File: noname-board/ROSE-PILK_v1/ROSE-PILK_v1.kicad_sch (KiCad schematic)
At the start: 2 parts, among them J2 Conn_01x03, SW1 SW_Push

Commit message: dual rp2040z
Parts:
- added J2: Conn_01x03, Connector_PinHeader_2.00mm:PinHeader_1x03_P2.00mm_Horizontal, symbol Connector_Generic:Conn_01x03
- added SW2: SW_Push, PS1024ALRED:SW_PS1024ALRED, symbol Switch:SW_Push
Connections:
- net GND: now also J2.2 (Pin_2), SW2.2
- net RP2040/SWCLK renamed SWDIO-A
- net RP2040/SWDIO renamed SWCLK-A
- new net RP2041/~{RST}: SW2.1
- new net SWCLK-B: J2.1 (Pin_1)
- new net SWDIO-B: J2.3 (Pin_3)
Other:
- added sheet BOOTSEL1 (BOOTSEL.kicad_sch)
- added sheet Flash Memory1 (flash.kicad_sch)
- added sheet RP2040-Connect (RP2040-Connect.kicad_sch)
- added sheet RP2041 (RP2040.kicad_sch)
- sheet USBC ports: added A-USB_D+, A-USB_D-, B-USB_D+, B-USB_D-; removed USB_D+, USB_D-
- note added: "RP2040-A"
- note added: "RP2040-A Comm Pins"
- note added: "RP2040-B"
- note added: "RP2040-B Comm Pins"
- note added: "SD Card Reader"
- moved on the sheet: J2

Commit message: Schematics
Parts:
- J2: footprint Connector_PinHeader_2.00mm:PinHeader_1x03_P2.00mm_Horizontal -> Connector_PinHeader_2.00mm:PinHeader_1x03_P2.00mm_Vertical
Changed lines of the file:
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@@
       (effects (font (size 1.27 1.27)))
     )
-    (property "Footprint" "Connector_PinHeader_2.00mm:PinHeader_1x03_P2.00mm_Horizontal" (at 270.51 73.66 0)
+    (property "Footprint" "Connector_PinHeader_2.00mm:PinHeader_1x03_P2.00mm_Vertical" (at 270.51 73.66 0)
       (effects (font (size 1.27 1.27)) hide)
     )
@@
       (effects (font (size 1.27 1.27)))
     )
-    (property "Footprint" "Connector_PinHeader_2.00mm:PinHeader_1x03_P2.00mm_Horizontal" (at 60.96 74.93 0)
+    (property "Footprint" "Connector_PinHeader_2.00mm:PinHeader_1x03_P2.00mm_Vertical" (at 60.96 74.93 0)
       (effects (font (size 1.27 1.27)) hide)
     )

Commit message: v1 functionality finished
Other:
- sheet USBC ports: added USB_5V; removed none
- sheet power ports: added USB_IN; removed none
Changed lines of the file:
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@@
+    (stroke (width 0) (type default))
+  )
+  (wire (pts (xy 36.83 72.39) (xy 41.91 72.39))
     (stroke (width 0) (type default))
   )
@@
   )
   (wire (pts (xy 68.58 111.76) (xy 81.28 111.76))
+    (stroke (width 0) (type default))
+  )
+  (wire (pts (xy 17.78 147.32) (xy 25.4 147.32))
     (stroke (width 0) (type default))
   )
@@
     (effects (font (size 1.27 1.27)) (justify right bottom))
   )
+  (label "USB_5V" (at 17.78 147.32 0) (fields_autoplaced)
+    (effects (font (size 1.27 1.27)) (justify left bottom))
+  )
   (label "3V3" (at 134.62 24.13 0) (fields_autoplaced)
     (effects (font (size 1.27 1.27)) (justify left bottom))
@@
   )
   (label "GPIO1-A" (at 175.26 27.94 0) (fields_autoplaced)
+    (effects (font (size 1.27 1.27)) (justify left bottom))
+  )
+  (label "USB_5V" (at 41.91 72.39 0) (fields_autoplaced)
     (effects (font (size 1.27 1.27)) (justify left bottom))
   )
@@
       (effects (font (size 1.27 1.27)) (justify right))
     )
+    (pin "USB_5V" input (at 36.83 72.39 0)
+      (effects (font (size 1.27 1.27)) (justify right))
+    )
     (instances
       (project "ROSE-PILK_v1"
@@
       (effects (font (size 1.27 1.27)) (justify left top))
     )
+    (pin "USB_IN" input (at 25.4 147.32 180)
+      (effects (font (size 1.27 1.27)) (justify left))
+    )
     (pin "5V" input (at 39.37 144.78 0)

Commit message: v1 functionality finished
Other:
- added sheet GPIO_Connect (GPIO_Connect.kicad_sch)

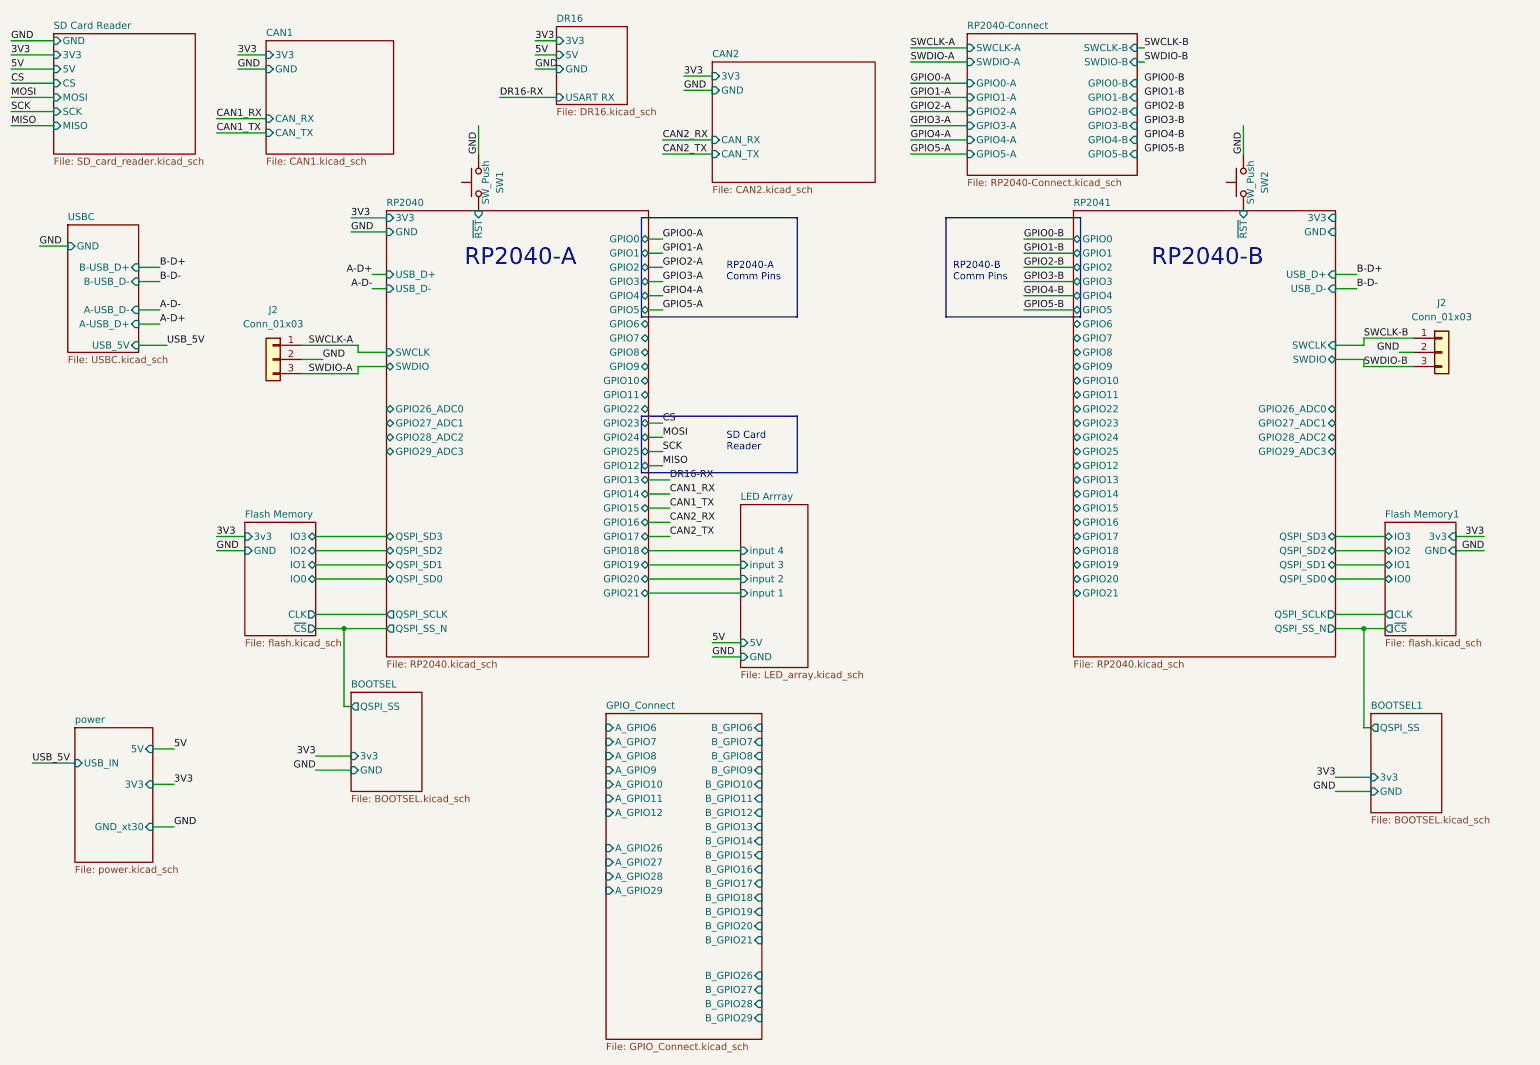
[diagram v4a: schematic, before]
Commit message: schematic finished, placement progress
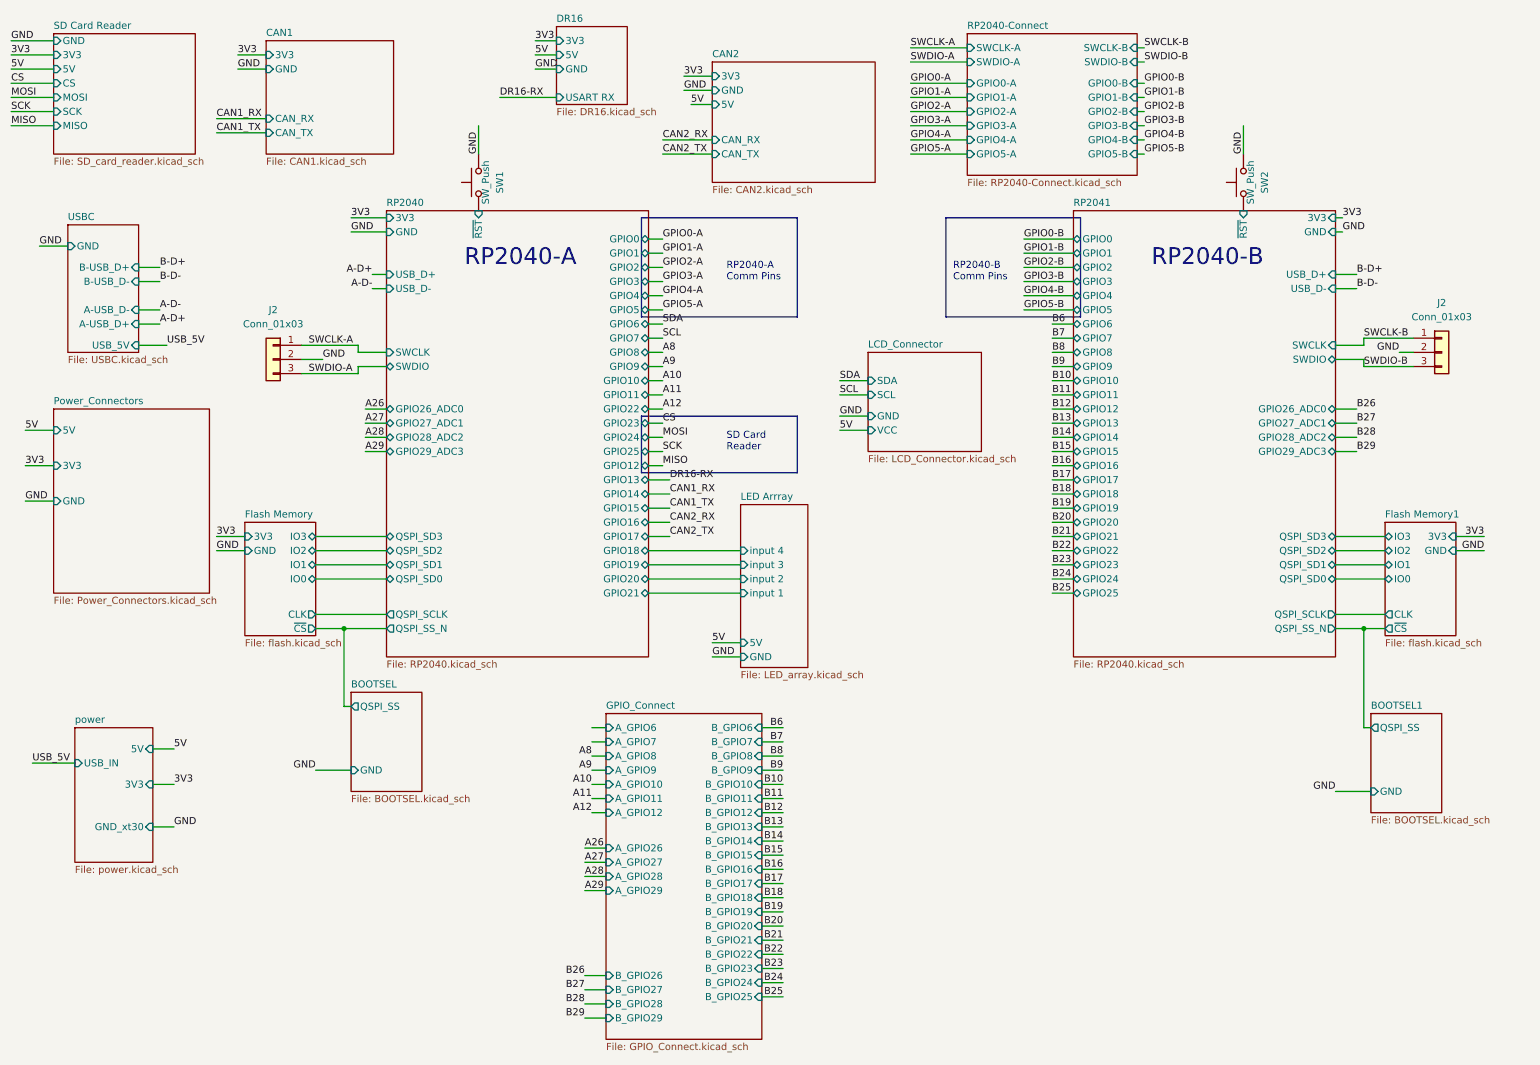
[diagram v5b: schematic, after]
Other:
- added sheet LCD_Connector (LCD_Connector.kicad_sch)
- added sheet Power_Connectors (Power_Connectors.kicad_sch)
- sheet BOOTSEL ports: added none; removed 3v3
- sheet BOOTSEL1 ports: added none; removed 3v3
- sheet CAN2 ports: added 5V; removed none
- sheet Flash Memory ports: added 3V3; removed 3v3
- sheet Flash Memory1 ports: added 3V3; removed 3v3
- sheet GPIO_Connect ports: added B_GPIO22, B_GPIO23, B_GPIO24, B_GPIO25; removed none

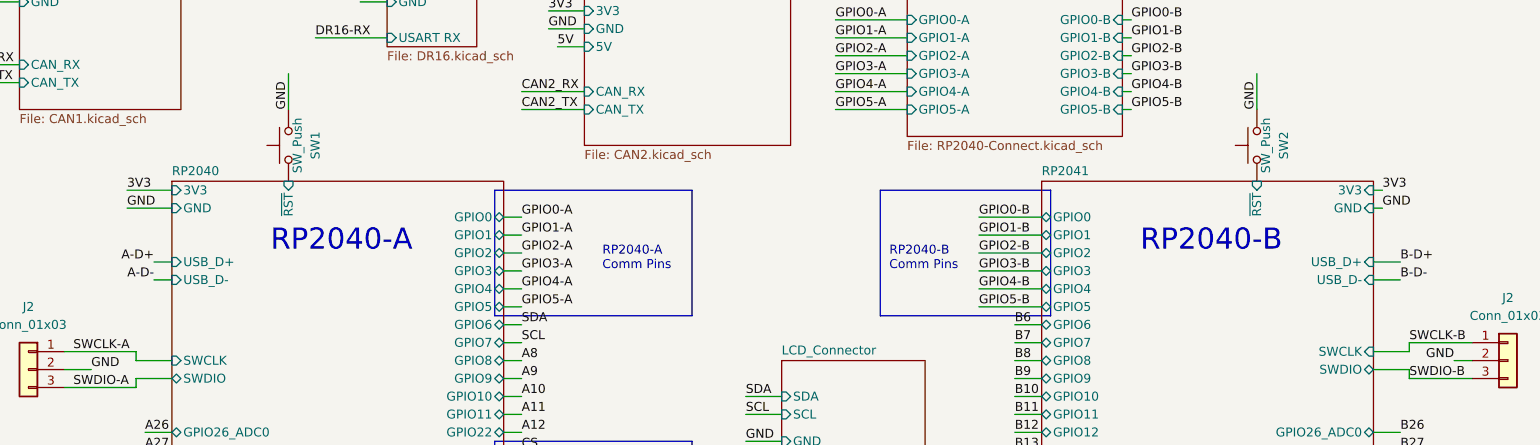
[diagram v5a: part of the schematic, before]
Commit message: ADDED 1V1 TO RP2040
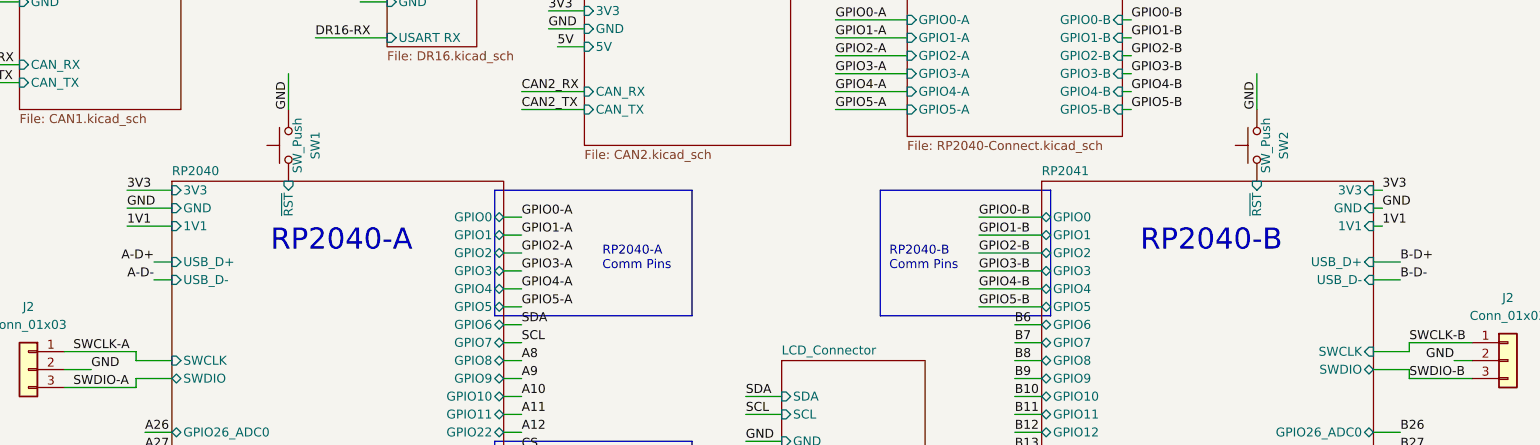
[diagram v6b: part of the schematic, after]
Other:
- sheet RP2040 ports: added 1V1; removed none
- sheet RP2041 ports: added 1V1; removed none
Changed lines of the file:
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@@
+    (stroke (width 0) (type default))
+  )
+  (wire (pts (xy 251.46 54.61) (xy 252.73 54.61))
     (stroke (width 0) (type default))
   )
@@
   )
   (wire (pts (xy 39.37 158.75) (xy 43.18 158.75))
+    (stroke (width 0) (type default))
+  )
+  (wire (pts (xy 74.93 54.61) (xy 81.28 54.61))
     (stroke (width 0) (type default))
   )
@@
     (effects (font (size 1.27 1.27)) (justify right bottom))
   )
+  (label "1V1" (at 252.73 54.61 0) (fields_autoplaced)
+    (effects (font (size 1.27 1.27)) (justify left bottom))
+  )
   (label "B17" (at 152.4 168.91 180) (fields_autoplaced)
     (effects (font (size 1.27 1.27)) (justify right bottom))
@@
   )
   (label "3V3" (at 54.61 20.32 0) (fields_autoplaced)
+    (effects (font (size 1.27 1.27)) (justify left bottom))
+  )
+  (label "1V1" (at 74.93 54.61 0) (fields_autoplaced)
     (effects (font (size 1.27 1.27)) (justify left bottom))
   )
@@
       (effects (font (size 1.27 1.27)) (justify right))
     )
+    (pin "1V1" input (at 81.28 54.61 180)
+      (effects (font (size 1.27 1.27)) (justify left))
+    )
     (instances
       (project "ROSE-PILK_v1"
@@
       (effects (font (size 1.27 1.27)) (justify left))
     )
-    (instances
+    (pin "1V1" input (at 251.46 54.61 0)
+      (effects (font (size 1.27 1.27)) (justify right))
+    )
+    (instances
